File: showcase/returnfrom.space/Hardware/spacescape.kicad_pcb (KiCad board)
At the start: 4 copper layers, 186 x 127.5 mm, 359 parts, among them J1 USB_C_Receptacle_USB2.0_16P, J15 Conn_02x04_Odd_Even, J19 Conn_01x08_Pin, J2 Conn_01x08_Socket, J20 Conn_01x08_Socket, J21 Conn_01x08_Socket, J22 USB_C_Receptacle_USB2.0_16P, J23 USB_C_Receptacle_USB2.0_16P, J24 Conn_02x04_Odd_Even, J25 Conn_01x02, J26 Conn_01x02, J27 Conn_01x02, J28 Conn_02x04_Odd_Even, J3 OLED, J4 Conn_02x04_Odd_Even, J5 Conn_02x04_Odd_Even, J6 OLED, J7 OLED, Q1 Crystal_GND24, Q2 NPN, Q3 NPN, Q4 NPN, Q5 NPN, SW0 SW_SPST, SW1 SW_SPST, SW10 SW_SPST, SW11 SW_SPST, SW12 SW_SPST, SW13 SW_SPST, SW14 SW_SPST, SW15 SW_SPST, SW16 SW_SPST, SW17 RESET, SW18 BOOTSEL, SW19 SW_SPST, SW2 SW_SPST, SW20 SW_SPST, SW21 SW_SPST, SW22 SW_SPST, SW23 SW_SPDT_321, SW24 SW_SPDT_321, SW25 BOOTSEL, SW26 SW_SPST, SW27 SW_SPST, SW28 SW_SPST, SW29 SW_SPST, SW3 SW_SPST, SW30 SW_SPST, SW31 SW_SPST, SW32 SW_SPST, SW33 SW_SPST, SW34 SW_SPST, SW35 SW_SPDT_321, SW36 BOOTSEL, SW37 RESET, SW38 RESET, SW4 SW_SPST, SW5 SW_SPST, SW6 SW_SPST, SW7 SW_SPST, SW8 SW_SPST, SW9 SW_SPST, U1 AMS1117-3.3, U10 TLV62565DBVx, U12 TP4056, U13 TLV62565DBVx, U14 FM8002, U15 LIS2DH, U16 LMA3722T421-OA5, U17 LMA3722T421-OA5, U18 TLV2372, U19 FM8002, U2 ESP32-S2-MINI-1, U3 RP2040, U4 MT3608L, U5 TLV2372, U6 TP4056, U7 LIS2DH, U8 W25Q128JVS, U9 ESP32-S2-MINI-2

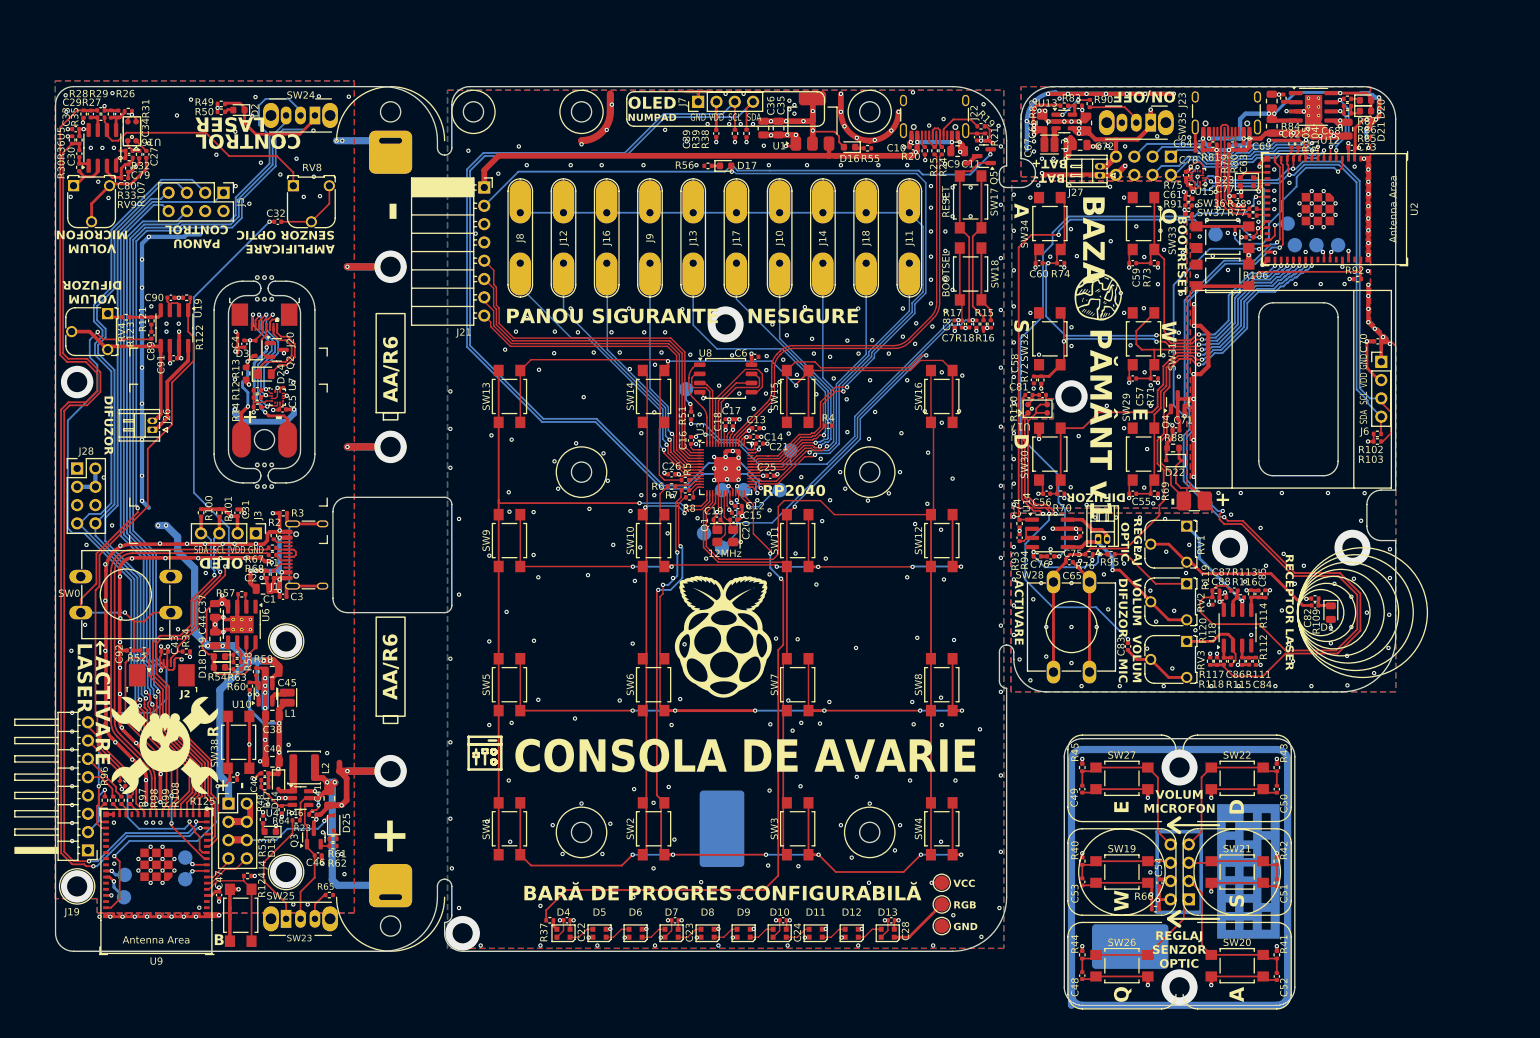
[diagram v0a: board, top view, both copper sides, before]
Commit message: Done. Ordered 50pcs. TO DO: clean-up, add BOM & POS
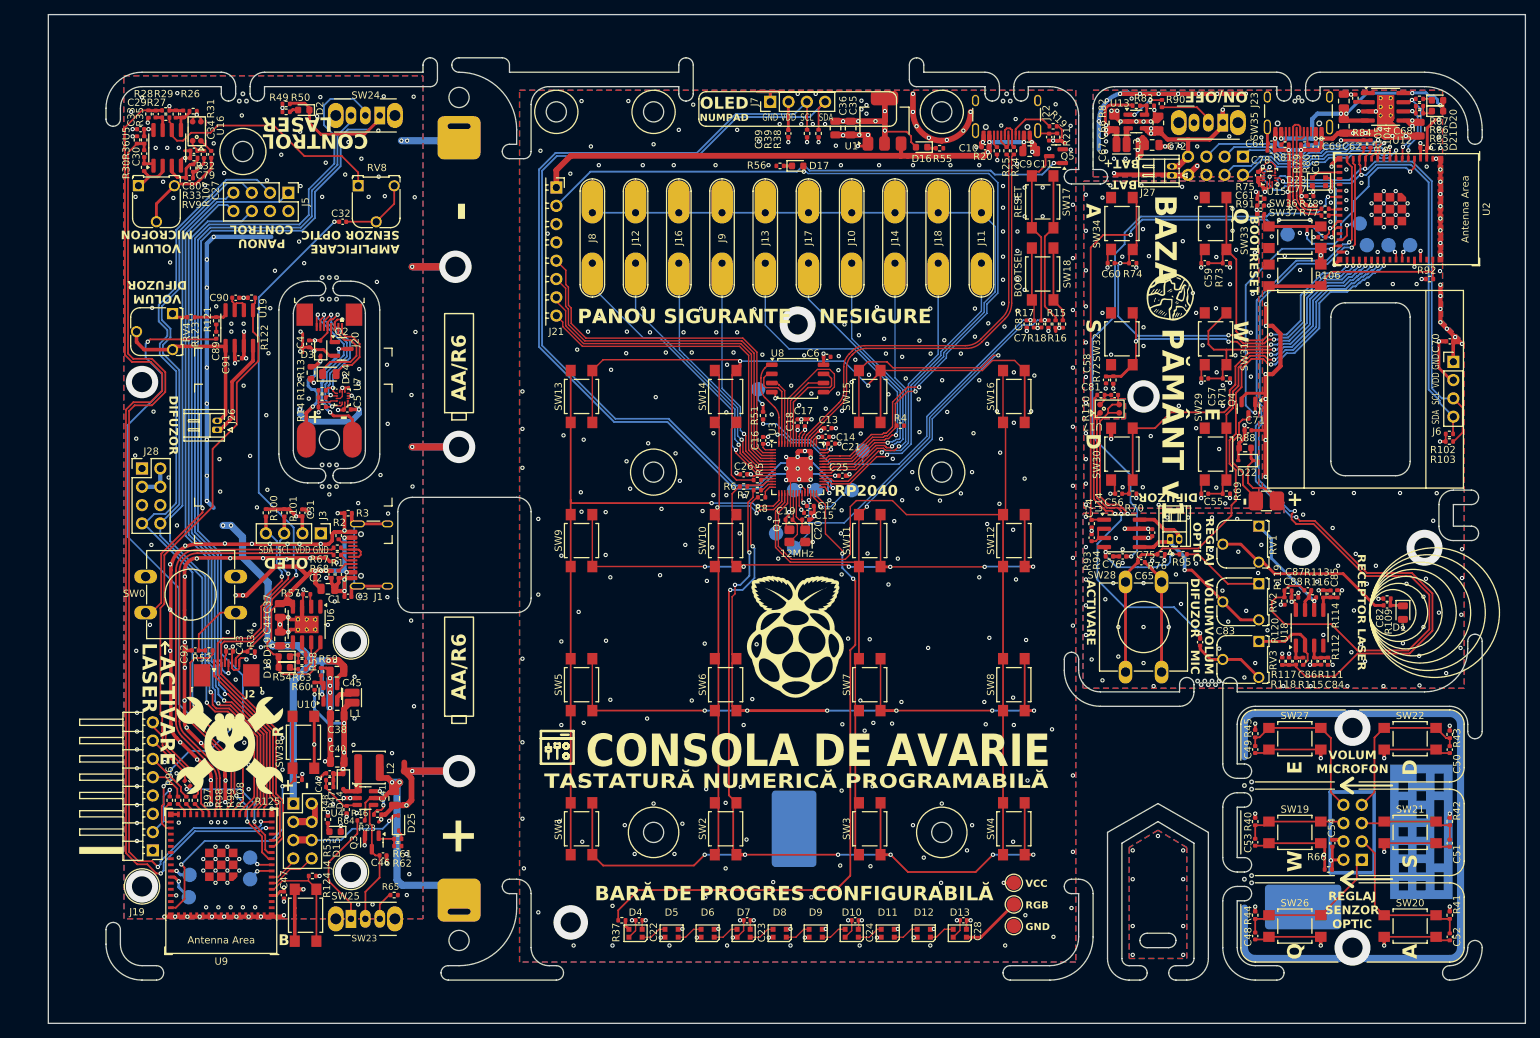
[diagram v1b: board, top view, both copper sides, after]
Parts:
- Q2, Q3, Q4, Q5: value NPN -> BC817
- moved C48 24.6 mm to (187.5, 147.9)
- moved C49 24.6 mm to (187.5, 122.0)
- moved C50 24.6 mm to (214.5, 122.0)
- moved C51 24.6 mm to (214.5, 135.0)
- moved C52 24.6 mm to (214.5, 148.0)
- moved C53 24.6 mm to (187.5, 134.9)
- moved C54 24.6 mm to (198.2, 135.0)
- moved J15 24.6 mm to (202.3, 137.3)
- moved R40 24.6 mm to (187.5, 132.0)
- moved R41 24.6 mm to (214.5, 145.0)
- moved R42 24.6 mm to (214.5, 132.0)
- moved R44 24.6 mm to (187.5, 145.0)
- moved R66 24.6 mm to (197.7, 138.7)
- moved SW19 24.6 mm to (193.0, 133.5)
- moved SW20 24.6 mm to (209.0, 146.5)
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- renumbered RGB+1 to 3V3, RGB-1 to GND3
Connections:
- net VBAT renamed +BATT
- Q2 pad 1: Net-(Q2-C) -> Net-(J20-Pin_4)
- Q2 pad 2: Net-(J20-Pin_4) -> GND
- Q2 pad 3: GND -> Net-(Q2-C)
- Q3 pad 1: /motherboard/EN2 -> Net-(Q3-B)
- Q3 pad 2: Net-(Q3-B) -> GND
- Q3 pad 3: GND -> /motherboard/EN2
- Q4 pad 1: Net-(Q4-C) -> LASER2_EN
- Q4 pad 2: LASER2_EN -> GND
- Q4 pad 3: GND -> Net-(Q4-C)
- Q5 pad 1: /numpad/RST1 -> Net-(J21-Pin_2)
- Q5 pad 2: Net-(J21-Pin_2) -> GND
- Q5 pad 3: GND -> /numpad/RST1
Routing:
- net +5V: track 223.7 -> 235.9 mm, vias 15 -> 16
- net GND: track 805.7 -> 796.4 mm, vias 704 -> 768
- net Net-(D2-K): track 128.5 -> 134.5 mm, vias 2 -> 1
- net Net-(J22-SHIELD): track 24.6 -> 20.1 mm
- net +3V0: track 42.2 -> 38.5 mm
- net +3V3: track 224.7 -> 222.0 mm, vias 86 -> 85
- net Net-(J20-Pin_4): track 4.61 -> 2.50 mm
- net Net-(J2-Pin_5): track 104.6 -> 106.2 mm
- net ADC1: track 137.2 -> 138.6 mm
- net Net-(D3-K): track 14.2 -> 15.6 mm
- net Net-(U9-GPIO6/ADC1_CH5): track 20.4 -> 19.0 mm
- net Net-(Q3-B): track 2.30 -> 3.55 mm
- net Net-(J21-Pin_2): track 74.8 -> 73.6 mm
- net /motherboard/SDA2: track 55.6 -> 56.5 mm
- net /motherboard/K3: track 102.0 -> 102.9 mm
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- added copper zone on In2.Cu, net GND
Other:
- board size 186 x 127.5 mm -> 205 x 140 mm
- board text added: "PANOU CONTROL SIGMA V1.0"
- board text added: "TASTATURĂ NUMERICĂ PROGRAMABILĂ"
- board text removed: "PANOU CONTROL SIGMA"
